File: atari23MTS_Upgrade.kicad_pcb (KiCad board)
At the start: 2 copper layers, 136 x 88 mm, 71 parts, among them P1 CONN_01X01, P2 CONN_01X01, P3 CONN_01X01, P4 CONN_01X01, P5 CONN_01X01, P6 CONN_01X01, SW1 SW_PUSH, U1 NCP1117ST33T3G, U10 TXB0108-PW, U11 ISSI61WV5128BL, U12 ISSI61WV5128BL, U13 ISSI61WV5128BL, U14 ISSI61WV5128BL, U15 74LS08, U16 74LS08, U2 STM32F401RCTx, U3 74LS138, U4 TXB0108-PW, U5 TXB0108-PW, U6 TXB0108-PW, U7 74HC04, U8 TXB0108-PW, U9 74LS32

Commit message: Transformation will begin shortly... ;-)
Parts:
- removed G***: LOGO, RetroBitLab:atari_fuji_SilkScreen_21.2x25-Rev
- removed REF**: Symbol_GNU-GPL_CopperTop_Small, Symbols:Symbol_GNU-GPL_CopperTop_Small
- removed XT1: 8Mhz, Crystals:Crystal_SMD_0603_4Pads
- added C14: 100n, Capacitors_SMD:C_1206_HandSoldering, F.Cu at (104.1, 100.3)
- added C15: 100n, Capacitors_SMD:C_1206_HandSoldering, F.Cu at (177.8, 90.8)
- added C16: 100n, Capacitors_SMD:C_1206_HandSoldering, F.Cu at (111.8, 101.6)
- added C17: 100n, Capacitors_SMD:C_1206_HandSoldering, F.Cu at (141.0, 74.9)
- added D4: LED.AMBER, LEDs:LED_1206, F.Cu at (89.5, 77.5)
- added D5: LED.RED, LEDs:LED_1206, F.Cu at (123.2, 54.6)
- added J1: Micro_SD_Card_Det, RetroBitLab:microSD_HC_Hirose_DM3D-SF, F.Cu at (144.8, 57.1)
- added R17: 0, Resistors_SMD:R_1206_HandSoldering, F.Cu at (137.2, 109.2)
- added R20: 220, Resistors_SMD:R_1206_HandSoldering, F.Cu at (115.6, 54.6)
- added U17: STM32F407VETx, Housings_QFP:LQFP-100_14x14mm_Pitch0.5mm, F.Cu at (127.0, 80.0)
- added U18: 74LS08, Housings_SSOP:TSSOP-14_4.4x5mm_Pitch0.65mm, F.Cu at (162.6, 97.8)
- added Y1: 8Mhz, Crystal:Crystal_SMD_0603-4Pin_6.0x3.5mm_HandSoldering, F.Cu at (115.6, 91.4)
- C4, C5: value C_Small -> 20p
- CART1: footprint ATARI-LEFT-CARTRIDGE -> RetroBitLab:ATARI-LEFT-CARTRIDGE
- D3: value ACT -> LED.GREEN
- P2, P3, P4, P5: footprint Connect:1pin -> RetroBitLab:MountingHole
- R10, R4: value 2.2k -> 220
- R11, R12: value 0 -> 10k
- R18: value 0 -> 47k
- R6, R7, R8, R9: value 10K -> 0
- U2: value STM32F401RCTx -> 74HC04; footprint Housings_QFP:LQFP-64_10x10mm_Pitch0.5mm -> Housings_SSOP:TSSOP-14_4.4x5mm_Pitch0.65mm
- U9: value 74LS32 -> 74HC04; footprint Housings_SSOP:SSOP-14_5.3x6.2mm_Pitch0.65mm -> Housings_SSOP:TSSOP-14_4.4x5mm_Pitch0.65mm
- moved R13 129.0 mm to (215.9, 62.2), turned to 90 degrees
- moved P6 121.8 mm to (208.3, 115.6)
- moved R12 107.6 mm to (215.9, 71.1), turned to 90 degrees
- moved R5 101.6 mm to (215.9, 80.0), turned to 90 degrees
- moved C6 80.4 mm to (215.9, 88.9), turned to 90 degrees
- moved R6 80.3 mm to (153.7, 120.7), turned to 0 degrees
- moved R7 79.1 mm to (161.3, 120.7), turned to 0 degrees
- moved C9 78.3 mm to (185.4, 95.2), turned to 0 degrees
- moved EXTPWR1 68.3 mm to (96.5, 111.8), turned to 180 degrees
- moved U9 65.8 mm to (94.0, 97.8), turned to 0 degrees
- moved U10 63.1 mm to (108.0, 74.9), turned to 0 degrees
- moved U15 63.1 mm to (174.0, 97.8), turned to 0 degrees
- moved R3 62.3 mm to (158.8, 66.0), turned to 0 degrees
- moved U7 53.3 mm to (94.0, 87.6), turned to 0 degrees
- moved U5 51.7 mm to (116.8, 63.5), turned to 0 degrees
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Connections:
- D3 pad 1: Net-(D3-Pad1) -> GND
- EXTPWR1 pad 4: Net-(EXTPWR1-Pad4) -> (no net)
- P2 pad 1: Net-(P2-Pad1) -> (no net)
- P3 pad 1: Net-(P3-Pad1) -> (no net)
- P4 pad 1: Net-(P4-Pad1) -> (no net)
- P5 pad 1: Net-(P5-Pad1) -> (no net)
- R10 pad 1: RAMEN -> Net-(D5-Pad2)
- R10 pad 2: GND -> LEDRED
- R11 pad 1: Net-(R11-Pad1) -> VCC3V3
- R11 pad 2: GND -> UART_RX_TTL
- R12 pad 1: Net-(R12-Pad1) -> VCC3V3
- R12 pad 2: GND -> UART_TX_TTL
- R13 pad 2: Net-(R13-Pad2) -> /MCU/SPARE1
- R14 pad 1: Net-(R14-Pad1) -> GND
- R14 pad 2: GND -> /MCU/SPARE2
- R15 pad 2: Net-(R15-Pad2) -> /MCU/SPARE3
- R16 pad 1: Net-(R16-Pad1) -> GND
- R16 pad 2: GND -> /MCU/SPARE4
- R18 pad 1: GND -> VCC3V3
- R18 pad 2: Net-(R18-Pad2) -> mSDO
- R19 pad 2: GND -> Net-(C4-Pad1)
- R4 pad 1: Net-(R4-Pad1) -> Net-(D3-Pad2)
- R4 pad 2: GND -> LEDGRN
- R5 pad 1: VCC3V3 -> Net-(D4-Pad2)
- R5 pad 2: Net-(D3-Pad2) -> LEDAMBER
- R6 pad 1: VCC3V3 -> GND
- R6 pad 2: UART_TX_TTL -> Net-(R6-Pad2)
- R7 pad 1: VCC3V3 -> GND
- R7 pad 2: UART_RX_TTL -> Net-(R7-Pad2)
- R8 pad 1: VCC3V3 -> GND
- R8 pad 2: Net-(R4-Pad1) -> Net-(R8-Pad2)
- R9 pad 1: VCC3V3 -> GND
- R9 pad 2: RAMEN -> Net-(R9-Pad2)
- U11 pad 1: PB3 -> mD1E2_A17
- U11 pad 2: PB2 -> mD1E2_A16
- U11 pad 23: mA10 -> mD1E0_A10
- U11 pad 25: mA11 -> mD1E0_A11
- U11 pad 26: mA9 -> mD1E0_A9
- U11 pad 27: mA8 -> mD1E0_A8
- U11 pad 28: mA13 -> mD1E0_A13
- U11 pad 3: PB0 -> mD1E0_A14
- U11 pad 30: PB4 -> mD1E2_A18
- U11 pad 31: PB1 -> mD1E0_A15
- U11 pad 4: mA12 -> mD1E0_A12
- U12 pad 1: PB3 -> mD1E2_A17
- U12 pad 2: PB2 -> mD1E2_A16
- U12 pad 23: mA10 -> mD1E0_A10
- U12 pad 25: mA11 -> mD1E0_A11
- U12 pad 26: mA9 -> mD1E0_A9
- U12 pad 27: mA8 -> mD1E0_A8
- U12 pad 28: mA13 -> mD1E0_A13
- U12 pad 3: PB0 -> mD1E0_A14
- U12 pad 30: PB4 -> mD1E2_A18
- U12 pad 31: PB1 -> mD1E0_A15
- U12 pad 4: mA12 -> mD1E0_A12
- U13 pad 1: PB3 -> mD1E2_A17
- U13 pad 2: PB2 -> mD1E2_A16
- U13 pad 23: mA10 -> mD1E0_A10
- U13 pad 25: mA11 -> mD1E0_A11
- U13 pad 26: mA9 -> mD1E0_A9
- U13 pad 27: mA8 -> mD1E0_A8
- U13 pad 28: mA13 -> mD1E0_A13
- U13 pad 3: PB0 -> mD1E0_A14
- U13 pad 30: PB4 -> mD1E2_A18
- U13 pad 31: PB1 -> mD1E0_A15
- U13 pad 4: mA12 -> mD1E0_A12
- U14 pad 1: PB3 -> mD1E2_A17
- U14 pad 2: PB2 -> mD1E2_A16
- U14 pad 23: mA10 -> mD1E0_A10
- U14 pad 25: mA11 -> mD1E0_A11
- U14 pad 26: mA9 -> mD1E0_A9
- U14 pad 27: mA8 -> mD1E0_A8
- U14 pad 28: mA13 -> mD1E0_A13
- U14 pad 3: PB0 -> mD1E0_A14
- U14 pad 30: PB4 -> mD1E2_A18
- U14 pad 31: PB1 -> mD1E0_A15
- U14 pad 4: mA12 -> mD1E0_A12
- U15 pad 10: mA15 -> ~mA13
- U15 pad 11: Net-(U15-Pad11) -> ~mA11mA9
- U15 pad 12: Net-(R11-Pad1) -> ~mA11
- U15 pad 13: Net-(R12-Pad1) -> mA9
- U15 pad 2: mA15 -> mA14
- U15 pad 5: Net-(U15-Pad5) -> mA12
- U15 pad 8: Net-(U15-Pad5) -> mDXXX
- U15 pad 9: mA15 -> Net-(U15-Pad6)
- U16 pad 1: ~mA13 -> mA10
- U16 pad 10: Net-(U16-Pad10) -> mA8
- U16 pad 11: Net-(U16-Pad11) -> mX6XX
- U16 pad 12: Net-(U15-Pad6) -> Net-(U16-Pad12)
- U16 pad 13: mA15 -> ~mA11mA9
- U16 pad 2: ~mA11 -> ~mA8
- U16 pad 3: Net-(U16-Pad3) -> Net-(U16-Pad12)
- U16 pad 4: Net-(U16-Pad3) -> ~mA11mA9
- U16 pad 5: ~mA10 -> Net-(U16-Pad5)
- U16 pad 6: Net-(U16-Pad10) -> mX3XX
- U16 pad 8: mD3XX -> Net-(U16-Pad5)
- U16 pad 9: Net-(U16-Pad11) -> ~mA10
- U2 pad 1: Net-(U2-Pad1) -> (no net)
- U2 pad 10: mA2 -> (no net)
- U2 pad 11: mA3 -> (no net)
- U2 pad 12: GND -> (no net)
- U2 pad 13: VCC3V3 -> (no net)
- U2 pad 14: TP1 -> VCC3V3
- U2 pad 2: Net-(U2-Pad2) -> (no net)
- U2 pad 3: Net-(U2-Pad3) -> (no net)
- U2 pad 4: Net-(U2-Pad4) -> (no net)
- U2 pad 5: Net-(C4-Pad1) -> (no net)
- U2 pad 6: Net-(C5-Pad1) -> (no net)
- U2 pad 7: nRESET -> GND
- U2 pad 8: mA0 -> (no net)
- U2 pad 9: mA1 -> (no net)
- U3 pad 1: PB5 -> mD1E2_A19
- U3 pad 10: Net-(U3-Pad10) -> (no net)
- U3 pad 11: Net-(U3-Pad11) -> (no net)
- U3 pad 2: PB6 -> mD1E3_A20
- U3 pad 3: PB7 -> mD1E3_A21
- U3 pad 4: ~ADDRSEL16K -> ~mD6XX
- U3 pad 5: ~ADDRSEL16K -> ~mD6XX
- U3 pad 7: Net-(U3-Pad7) -> (no net)
- U3 pad 9: Net-(U3-Pad9) -> (no net)
- U7 pad 1: mA14 -> mA10
- U7 pad 2: Net-(U7-Pad2) -> ~mA10
- U7 pad 8: ~mA10 -> ~mA8
- U7 pad 9: mA10 -> mA8
- U8 pad 12: Net-(U8-Pad12) -> (no net)
- U8 pad 13: Net-(U8-Pad13) -> (no net)
- U8 pad 8: Net-(U8-Pad8) -> (no net)
- U8 pad 9: Net-(U8-Pad9) -> (no net)
- U9 pad 1: Net-(U7-Pad2) -> mD6XX
- U9 pad 10: Net-(R16-Pad1) -> (no net)
- U9 pad 11: Net-(U9-Pad11) -> (no net)
- U9 pad 12: Net-(R13-Pad2) -> (no net)
- U9 pad 13: Net-(R14-Pad1) -> (no net)
- U9 pad 14: VCC3V3 -> (no net)
- U9 pad 2: mA15 -> ~mD6XX
- U9 pad 3: ~ADDRSEL16K -> (no net)
- U9 pad 4: Net-(R18-Pad2) -> (no net)
- U9 pad 5: Net-(R19-Pad1) -> (no net)
- U9 pad 6: Net-(U9-Pad6) -> (no net)
- U9 pad 7: GND -> (no net)
- U9 pad 8: Net-(U9-Pad8) -> (no net)
- U9 pad 9: Net-(R15-Pad2) -> (no net)
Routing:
- net GND: track 691.0 -> 0.00 mm, vias 2 -> 0
- net VCC3V3: track 466.9 -> 0.00 mm, vias 19 -> 0
- net +5VDC: track 234.2 -> 0.00 mm, vias 3 -> 0
- net mD7: track 200.4 -> 0.00 mm, vias 9 -> 0
- net mD5: track 189.0 -> 0.00 mm, vias 12 -> 0
- net mD4: track 188.6 -> 0.00 mm, vias 9 -> 0
- net mA1: track 186.7 -> 0.00 mm, vias 11 -> 0
- net VCC5V: track 186.2 -> 0.00 mm, vias 8 -> 0
- net mD0: track 183.2 -> 0.00 mm, vias 5 -> 0
- net mR/~W: track 176.9 -> 0.00 mm, vias 9 -> 0
- net mA13: track 171.9 -> 0.00 mm, vias 8 -> 0
- net mD3: track 170.7 -> 0.00 mm, vias 9 -> 0
- net RAMEN: track 170.4 -> 0.00 mm, vias 10 -> 0
- net mD6: track 168.4 -> 0.00 mm, vias 10 -> 0
- net mA3: track 166.6 -> 0.00 mm, vias 8 -> 0
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- removed copper zone on B.Cu, net GND
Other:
- board text removed: "5V GND GND 12V"
- board text removed: "8-BIT"
- board text removed: "ATARI XE 2/4 MEG RAM EXPANSION"
- board text removed: "GND"
- board text removed: "GND RX TX"
- board text removed: "Power Without the Price!"
- board text removed: "RBL001.AT01"
- board text removed: "RETROBIT LAB"
- board text removed: "designed by R.G. 2019"
- board text removed: "in memoriam A.S.-G.D."

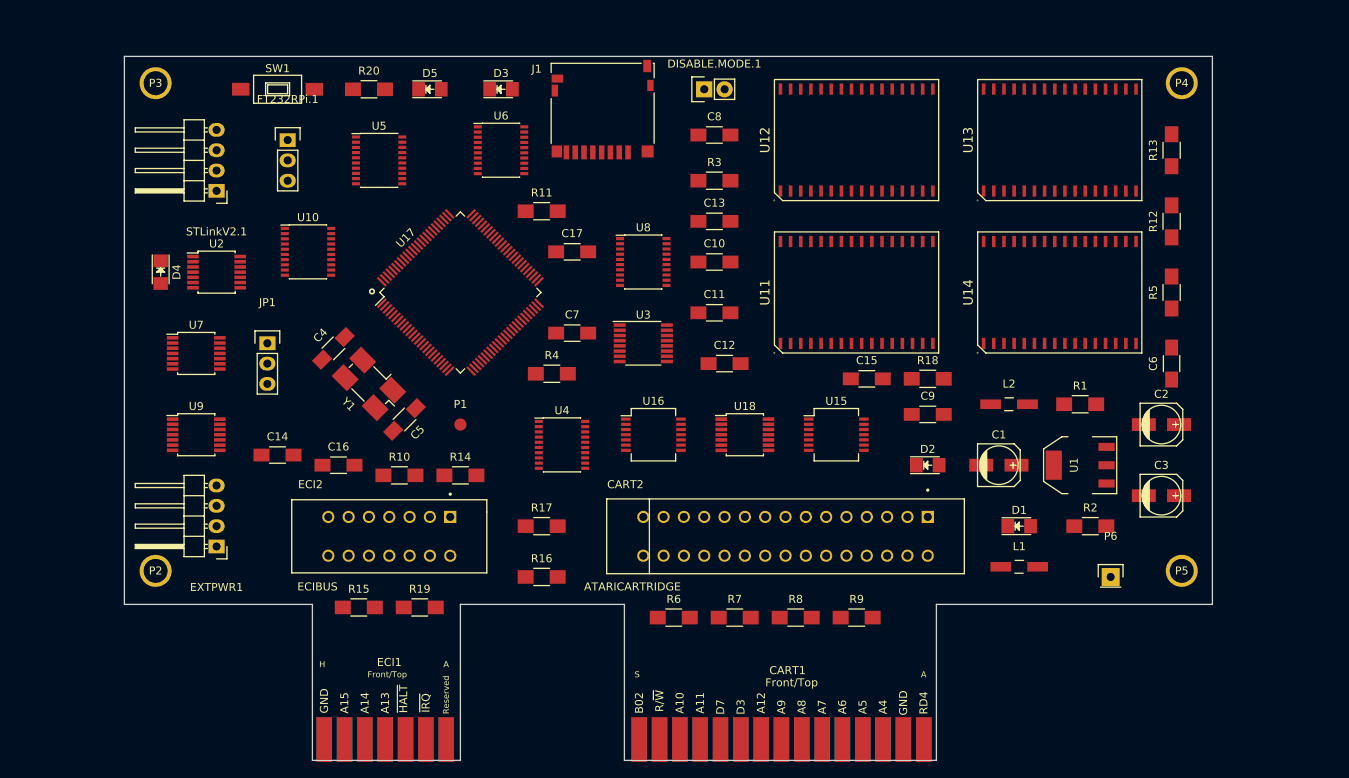
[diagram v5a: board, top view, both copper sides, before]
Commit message: Multiple library support for Kicad. Need a reconfiguration at work
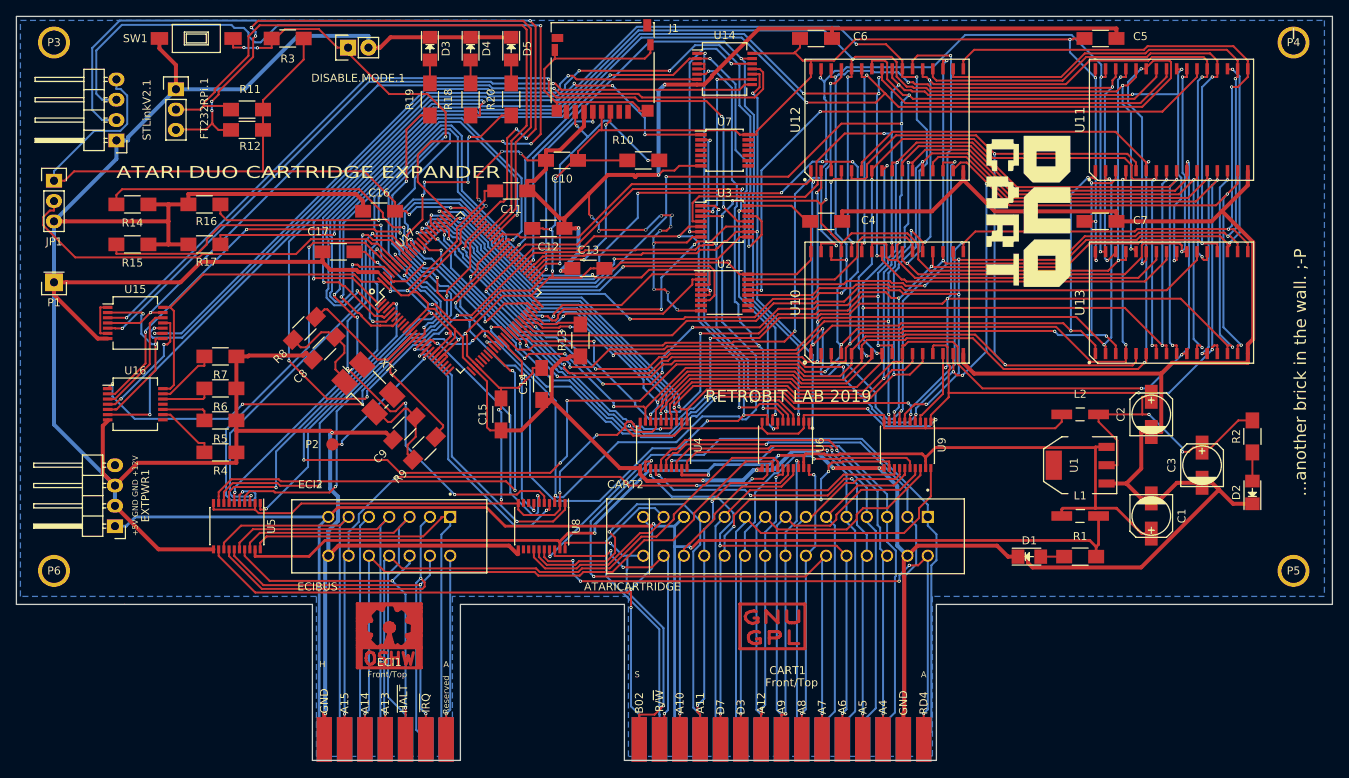
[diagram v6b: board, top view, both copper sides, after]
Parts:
- removed U18: 74LS08, Housings_SSOP:TSSOP-14_4.4x5mm_Pitch0.65mm
- removed Y1: 8Mhz, Crystal:Crystal_SMD_0603-4Pin_6.0x3.5mm_HandSoldering
- added ATARI LOGO FUJI: LOGO, RetroBitLab:atari_fuji_SilkScreen_21.2x25-RevBack, B.Cu at (154.0, 79.0)
- added DUOCART: LOGO, RetroBitLab:DUOCart_20x11_Rev, F.Cu at (198.0, 70.0)
- added REF**: Symbol_GNU-GPL_CopperTop_Small, Symbol:Symbol_GNU-GPL_CopperTop_Small, F.Cu at (166.0, 122.0)
- added REF**: Symbol_OSHW-Logo_CopperTop_Negative, Symbols:Symbol_OSHW-Logo_CopperTop_Negative, F.Cu at (118.1, 121.9)
- added XT1: 8Mhz, Crystal:Crystal_SMD_0603-4Pin_6.0x3.5mm_HandSoldering, F.Cu at (115.5, 92.0)
- C4, C5: value 20p -> 100n
- C8, C9: value 100n -> 20p
- D4: value LED.AMBER -> LED.RED
- D5: value LED.RED -> LED.AMBER
- P1: footprint Measurement_Points:Measurement_Point_Round-SMD-Pad_Small -> Pin_Headers:Pin_Header_Straight_1x01
- P2: footprint RetroBitLab:MountingHole -> Measurement_Points:Measurement_Point_Round-SMD-Pad_Small
- P6: footprint Pin_Headers:Pin_Header_Straight_1x01 -> RetroBitLab:MountingHole
- R10: value 220 -> 47k
- R18: value 47k -> 220
- R19, R9: value 0 -> 220
- R4, R5: value 220 -> 0
- U10: value TXB0108-PW -> ISSI61WV5128BL; footprint Housings_SSOP:SSOP-20_4.4x6.5mm_Pitch0.65mm -> RetroBitLab:SOP-32L-20.5x11.30-1.27mm
- U14: value ISSI61WV5128BL -> 74LS08; footprint RetroBitLab:SOP-32L-20.5x11.30-1.27mm -> Housings_SSOP:SSOP-14_5.3x6.2mm_Pitch0.65mm
- U2: value 74HC04 -> 74LS138; footprint Housings_SSOP:TSSOP-14_4.4x5mm_Pitch0.65mm -> Housings_SSOP:TSSOP-16_4.4x5mm_Pitch0.65mm
- U3: value 74LS138 -> 74HC04; footprint Housings_SSOP:TSSOP-16_4.4x5mm_Pitch0.65mm -> Housings_SSOP:TSSOP-14_4.4x5mm_Pitch0.65mm
- U9: value 74HC04 -> TXB0108-PW; footprint Housings_SSOP:TSSOP-14_4.4x5mm_Pitch0.65mm -> Housings_SSOP:SSOP-20_4.4x6.5mm_Pitch0.65mm
- moved P6 132.1 mm to (76.2, 114.3)
- moved R5 120.0 mm to (97.0, 96.0), turned to 180 degrees
- moved R12 116.1 mm to (100.3, 59.7), turned to 180 degrees
- moved C5 99.2 mm to (207.0, 48.3), turned to 0 degrees
- moved U9 88.9 mm to (182.9, 99.1), turned to 270 degrees
- moved U15 88.7 mm to (86.4, 83.8)
- moved R13 77.6 mm to (142.0, 86.0)
- moved U10 72.7 mm to (180.3, 81.3)
- moved R7 72.1 mm to (97.0, 88.0), turned to 180 degrees
- moved R18 71.4 mm to (123.2, 55.9), turned to 270 degrees
- moved R8 71.3 mm to (107.5, 84.5), turned to 225 degrees
- moved U7 70.8 mm to (160.0, 62.2)
- moved C7 67.5 mm to (207.0, 71.1)
- moved C9 65.4 mm to (120.0, 97.0), turned to 225 degrees
- moved U16 64.9 mm to (86.4, 94.0)
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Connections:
- C11 pad 1: VCC3V3 -> GND
- C11 pad 2: GND -> VCC3V3
- C12 pad 1: VCC3V3 -> GND
- C12 pad 2: GND -> VCC3V3
- C13 pad 1: VCC3V3 -> GND
- C13 pad 2: GND -> VCC3V3
- C17 pad 1: VCC3V3 -> GND
- C17 pad 2: GND -> VCC3V3
- C4 pad 1: Net-(C4-Pad1) -> VCC3V3
- C5 pad 1: Net-(C5-Pad1) -> VCC3V3
- C6 pad 1: GND -> VCC3V3
- C6 pad 2: VCC3V3 -> GND
- C7 pad 1: GND -> VCC3V3
- C7 pad 2: VCC3V3 -> GND
- C8 pad 1: GND -> Net-(C8-Pad1)
- C8 pad 2: VCC3V3 -> GND
- C9 pad 1: GND -> Net-(C9-Pad1)
- C9 pad 2: VCC3V3 -> GND
- P1 pad 1: TP1 -> GND
- P2 pad 1: (no net) -> TP1
- P6 pad 1: GND -> (no net)
- R10 pad 1: Net-(D5-Pad2) -> VCC3V3
- R10 pad 2: LEDRED -> mSDO
- R18 pad 1: VCC3V3 -> Net-(D3-Pad2)
- R18 pad 2: mSDO -> LEDGRN
- R19 pad 1: Net-(R19-Pad1) -> Net-(D4-Pad2)
- R19 pad 2: Net-(C4-Pad1) -> LEDRED
- R20 pad 1: Net-(R20-Pad1) -> Net-(D5-Pad2)
- R20 pad 2: Net-(C5-Pad1) -> LEDAMBER
- R4 pad 1: Net-(D3-Pad2) -> GND
- R4 pad 2: LEDGRN -> Net-(R4-Pad2)
- R5 pad 1: Net-(D4-Pad2) -> GND
- R5 pad 2: LEDAMBER -> Net-(R5-Pad2)
- R8 pad 1: GND -> Net-(R8-Pad1)
- R8 pad 2: Net-(R8-Pad2) -> Net-(C8-Pad1)
- R9 pad 1: GND -> Net-(R9-Pad1)
- R9 pad 2: Net-(R9-Pad2) -> Net-(C9-Pad1)
- U10 pad 1: mD0 -> mD1E2_A17
- U10 pad 10: VCC3V3 -> mA2
- U10 pad 11: GND -> mA1
- U10 pad 12: D7 -> mA0
- U10 pad 13: D6 -> mD0
- U10 pad 14: D5 -> mD1
- U10 pad 15: D4 -> mD2
- U10 pad 16: D3 -> GND
- U10 pad 17: D2 -> mD3
- U10 pad 18: D1 -> mD4
- U10 pad 19: VCC5V -> mD5
- U10 pad 2: VCC3V3 -> mD1E2_A16
- U10 pad 20: D0 -> mD6
- U10 pad 3: mD1 -> mD1E0_A14
- U10 pad 4: mD2 -> mD1E0_A12
- U10 pad 5: mD3 -> mA7
- U10 pad 6: mD4 -> mA6
- U10 pad 7: mD5 -> mA5
- U10 pad 8: mD6 -> mA4
- U10 pad 9: mD7 -> mA3
- U11 pad 22: ~BSEL0 -> ~BSEL2
- U12 pad 22: ~BSEL2 -> ~BSEL1
- U13 pad 22: ~BSEL1 -> ~BSEL3
- U14 pad 1: mD1E2_A17 -> mA15
- U14 pad 10: mA2 -> mA8
- U14 pad 11: mA1 -> ~mA11mA9
- U14 pad 12: mA0 -> ~mA11
- U14 pad 13: mD0 -> mA9
- U14 pad 14: mD1 -> VCC3V3
- U14 pad 2: mD1E2_A16 -> mA14
- U14 pad 3: mD1E0_A14 -> Net-(U14-Pad3)
- U14 pad 4: mD1E0_A12 -> Net-(U14-Pad3)
- U14 pad 5: mA7 -> mA12
- U14 pad 6: mA6 -> Net-(U14-Pad6)
- U14 pad 7: mA5 -> GND
- U14 pad 8: mA4 -> Net-(U14-Pad8)
- U14 pad 9: mA3 -> ~mA10
- U15 pad 1: mA15 -> mX3XX
- U15 pad 11: ~mA11mA9 -> mX6XX
- U15 pad 12: ~mA11 -> Net-(U15-Pad12)
- U15 pad 13: mA9 -> ~mA11mA9
- U15 pad 2: mA14 -> mDXXX
- U15 pad 3: Net-(U15-Pad3) -> mD3XX
- U15 pad 4: Net-(U15-Pad3) -> ~mA11mA9
- U15 pad 5: mA12 -> Net-(U14-Pad8)
- U15 pad 6: Net-(U15-Pad6) -> mX3XX
- U15 pad 9: Net-(U15-Pad6) -> Net-(U14-Pad6)
- U16 pad 10: mA8 -> Net-(R5-Pad2)
- U16 pad 11: mX6XX -> (no net)
- U16 pad 12: Net-(U16-Pad12) -> Net-(R6-Pad2)
- U16 pad 13: ~mA11mA9 -> Net-(R7-Pad2)
- U16 pad 3: Net-(U16-Pad12) -> Net-(U15-Pad12)
- U16 pad 4: ~mA11mA9 -> mX6XX
- U16 pad 5: Net-(U16-Pad5) -> mDXXX
- U16 pad 6: mX3XX -> mD6XX
- U16 pad 8: Net-(U16-Pad5) -> (no net)
- U16 pad 9: ~mA10 -> Net-(R4-Pad2)
- U17 pad 12: Net-(R19-Pad1) -> Net-(R8-Pad1)
- U17 pad 13: Net-(R20-Pad1) -> Net-(R9-Pad1)
- U2 pad 1: (no net) -> mD1E2_A19
- U2 pad 12: (no net) -> ~BSEL3
- U2 pad 13: (no net) -> ~BSEL2
- U2 pad 14: VCC3V3 -> ~BSEL1
- U2 pad 2: (no net) -> mD1E3_A20
- U2 pad 3: (no net) -> mD1E3_A21
- U2 pad 4: (no net) -> ~mD6XX
- U2 pad 5: (no net) -> ~mD6XX
- U2 pad 6: (no net) -> RAMEN
- U2 pad 7: GND -> (no net)
- U2 pad 8: (no net) -> GND
- U3 pad 1: mD1E2_A19 -> mA10
- U3 pad 10: (no net) -> ~mD3XX
- U3 pad 11: (no net) -> mD3XX
- U3 pad 12: ~BSEL3 -> ~mA13
- U3 pad 13: ~BSEL2 -> mA13
- U3 pad 14: ~BSEL1 -> VCC3V3
- U3 pad 2: mD1E3_A20 -> ~mA10
- U3 pad 3: mD1E3_A21 -> mR/~W
- U3 pad 4: ~mD6XX -> ~mOE
- U3 pad 5: ~mD6XX -> mA11
- U3 pad 6: RAMEN -> ~mA11
- U3 pad 7: (no net) -> GND
- U3 pad 8: GND -> ~mA8
- U3 pad 9: (no net) -> mA8
- U4 pad 1: ~mEXSEL -> mA0
- U4 pad 12: ~CCTL -> A7
- U4 pad 13: ~REF -> A6
- U4 pad 14: ~RST -> A5
- U4 pad 15: ~IRQ -> A4
- U4 pad 16: ~MPD -> A3
- U4 pad 17: ~HALT -> A2
- U4 pad 18: ~D1XX -> A1
- U4 pad 20: ~EXSEL -> A0
- U4 pad 3: ~mD1XX -> mA1
- U4 pad 4: ~mHALT -> mA2
- U4 pad 5: ~mMPD -> mA3
- U4 pad 6: ~mIRQ -> mA4
- U4 pad 7: ~mRST -> mA5
- U4 pad 8: ~mREF -> mA6
- U4 pad 9: ~mCCTL -> mA7
- U5 pad 1: mA0 -> ~mEXSEL
- U5 pad 12: A7 -> ~CCTL
- U5 pad 13: A6 -> ~REF
- U5 pad 14: A5 -> ~RST
- U5 pad 15: A4 -> ~IRQ
- U5 pad 16: A3 -> ~MPD
- U5 pad 17: A2 -> ~HALT
- U5 pad 18: A1 -> ~D1XX
- U5 pad 20: A0 -> ~EXSEL
- U5 pad 3: mA1 -> ~mD1XX
- U5 pad 4: mA2 -> ~mHALT
- U5 pad 5: mA3 -> ~mMPD
- U5 pad 6: mA4 -> ~mIRQ
- U5 pad 7: mA5 -> ~mRST
- U5 pad 8: mA6 -> ~mREF
- U5 pad 9: mA7 -> ~mCCTL
- U7 pad 1: mA10 -> mD6XX
- U7 pad 10: ~mD3XX -> (no net)
- U7 pad 11: mD3XX -> (no net)
- U7 pad 12: ~mA13 -> (no net)
- U7 pad 13: mA13 -> (no net)
- U7 pad 2: ~mA10 -> ~mD6XX
- U7 pad 3: mR/~W -> (no net)
- U7 pad 4: ~mOE -> (no net)
- U7 pad 5: mA11 -> (no net)
- U7 pad 6: ~mA11 -> (no net)
- U7 pad 8: ~mA8 -> (no net)
- U7 pad 9: mA8 -> (no net)
- U9 pad 1: mD6XX -> mD0
- U9 pad 10: (no net) -> VCC3V3
- U9 pad 11: (no net) -> GND
- U9 pad 12: (no net) -> D7
- U9 pad 13: (no net) -> D6
- U9 pad 14: (no net) -> D5
- U9 pad 2: ~mD6XX -> VCC3V3
- U9 pad 3: (no net) -> mD1
- U9 pad 4: (no net) -> mD2
- U9 pad 5: (no net) -> mD3
- U9 pad 6: (no net) -> mD4
- U9 pad 7: (no net) -> mD5
- U9 pad 8: (no net) -> mD6
- U9 pad 9: (no net) -> mD7
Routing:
- net GND: track 0.00 -> 910.3 mm, vias 0 -> 25
- net VCC3V3: track 0.00 -> 554.3 mm, vias 0 -> 20
- net mD1E0_A11: track 0.00 -> 205.7 mm, vias 0 -> 5
- net mD1E0_A8: track 0.00 -> 203.9 mm, vias 0 -> 6
- net mD1E0_A9: track 0.00 -> 196.5 mm, vias 0 -> 5
- net mD1E0_A10: track 0.00 -> 195.7 mm, vias 0 -> 6
- net mD1E0_A12: track 0.00 -> 193.5 mm, vias 0 -> 9
- net mD1E0_A14: track 0.00 -> 192.4 mm, vias 0 -> 9
- net mR/~W: track 0.00 -> 188.7 mm, vias 0 -> 8
- net +5VDC: track 0.00 -> 188.0 mm, vias 0 -> 2
- net mA2: track 0.00 -> 187.3 mm, vias 0 -> 5
- net mD4: track 0.00 -> 183.2 mm, vias 0 -> 5
- net mD1E0_A13: track 0.00 -> 183.0 mm, vias 0 -> 6
- net mD3: track 0.00 -> 183.0 mm, vias 0 -> 7
- net mD0: track 0.00 -> 182.4 mm, vias 0 -> 7
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- added copper zone on B.Cu, net GND
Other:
- board size 136 x 88 mm -> 164.5 x 93 mm
- net class +5VDC: via_dia 0.6 -> 0.4
- net class GND: via_dia 0.6 -> 0.4
- net class VCC5V: via_dia 0.6 -> 0.4
- board text added: "+5V GND GND +12V"
- board text added: "...another brick in the wall. ;-P"
- board text added: "8-BIT"
- board text added: "ATARI DUO CARTRIDGE EXPANDER"
- board text added: "RETROBIT LAB 2019"
- board text added: "designed by R.G.2019"
- board text added: "in memoriam A.S.-G.D."
- board text added: "power without the price!"
